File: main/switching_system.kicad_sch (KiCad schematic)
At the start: 5 parts

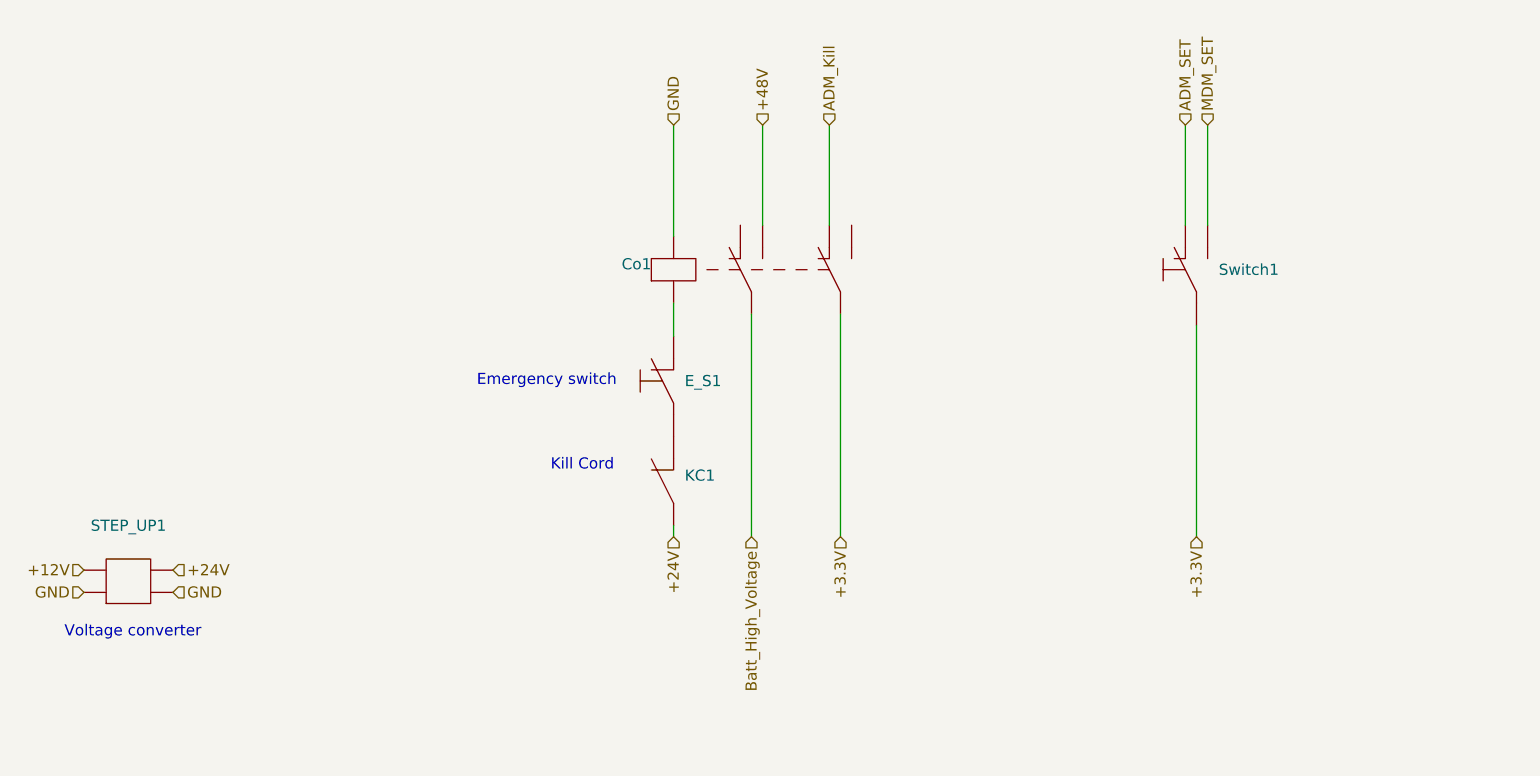
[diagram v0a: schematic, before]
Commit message: updated layout of switching system sheet, added powertrain symbol
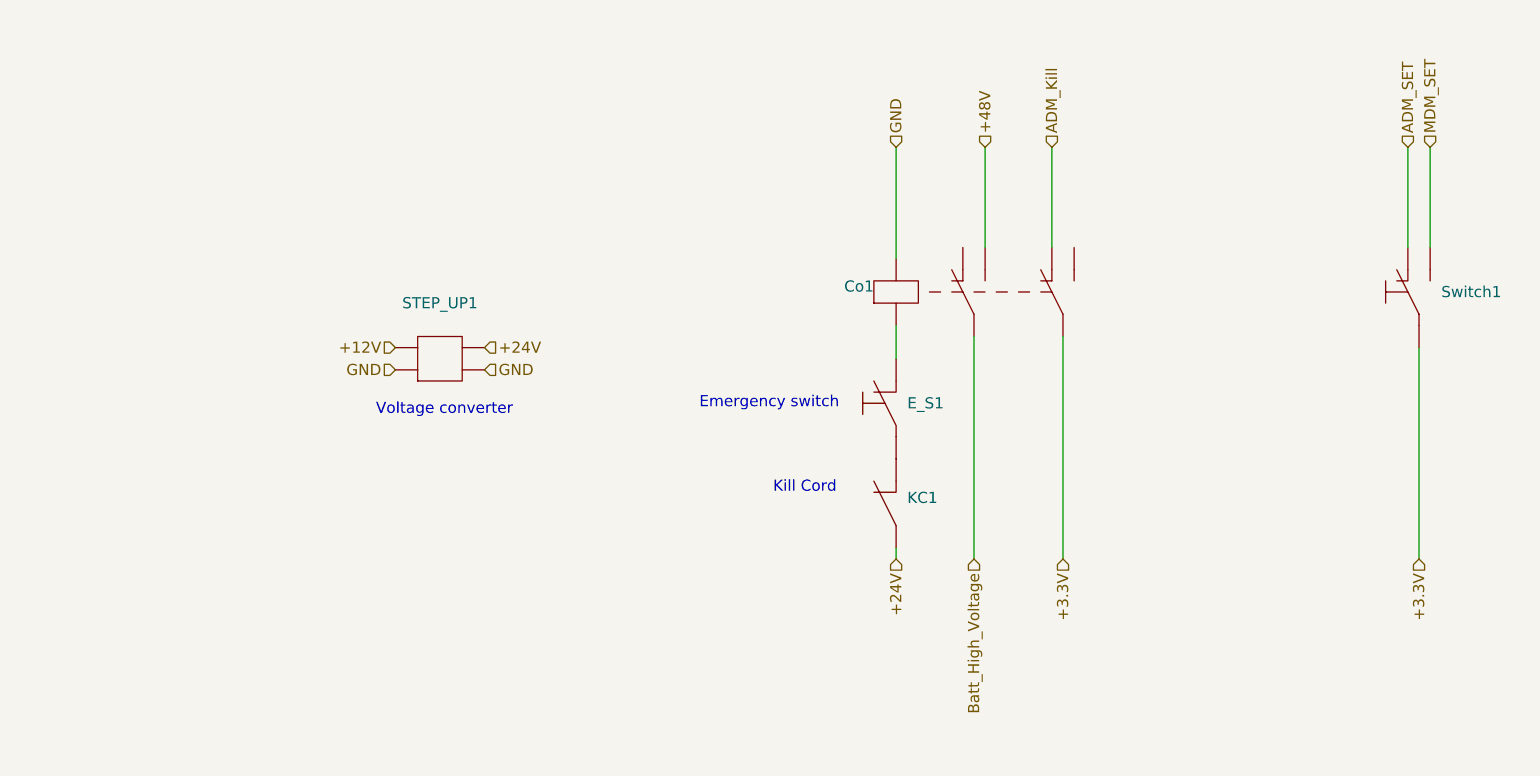
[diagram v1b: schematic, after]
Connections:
- net at E_S1.: now also KC1.; no longer Co1.
- new net: Co1., E_S1.
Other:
- moved on the sheet: Co1, E_S1, KC1, STEP_UP1, Switch1

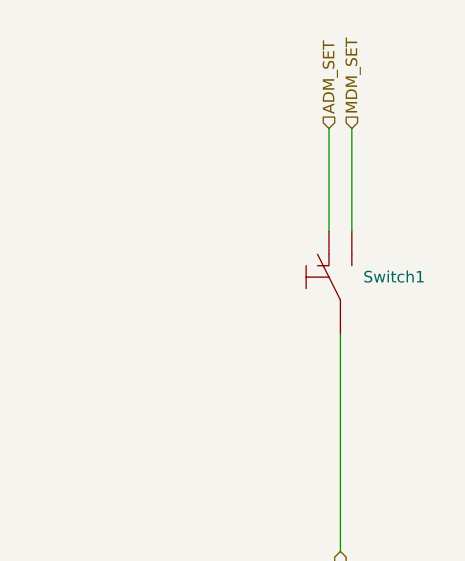
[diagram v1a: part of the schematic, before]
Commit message: removed AMS line, and previous switch ing UI. Renamed Switch in switching system to AMS
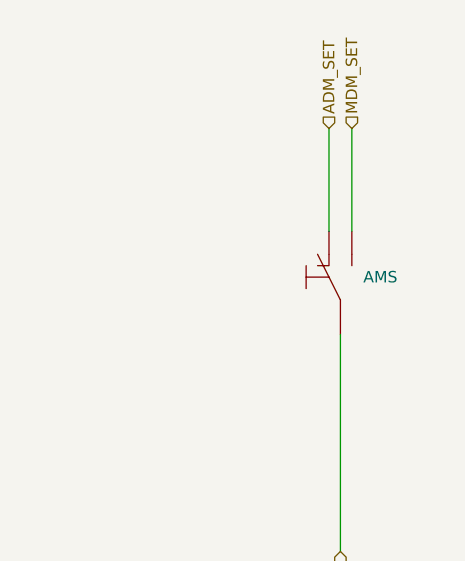
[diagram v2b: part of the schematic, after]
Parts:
- renumbered Switch1 to AMS
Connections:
- net at E_S1.: now also KC1.; no longer Co1.
- new net: Co1., E_S1.
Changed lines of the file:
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@@
 		(dnp no)
 		(fields_autoplaced yes)
-		(property "Reference" "Switch1"
+		(property "Reference" "AMS"
 			(at 209.55 86.3599 90)
 			(effects
@@
 			(project ""
 				(path "/54fbbba9-a737-4199-9a4b-f9fa49b3de5e/7cfabc18-403c-4549-890d-a8e23f0c0871"
-					(reference "Switch1")
+					(reference "AMS")
 					(unit 1)
 				)
